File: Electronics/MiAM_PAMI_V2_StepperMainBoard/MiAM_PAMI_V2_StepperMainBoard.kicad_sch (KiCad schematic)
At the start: 31 parts, among them J1 Conn_01x11_Male, J2 Conn_01x03_Male, J3 Conn_01x03_Male, U1 ESP32-DEVKITC-32U, U2 3V3, U3 MT3608, U4 LM7805_TO220

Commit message: Fix pcb & add driver board
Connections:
- net +3V3: now also J1.11 (Pin_11); no longer J1.10 (Pin_10)
- net DIR_1: now also J1.7 (Pin_7); no longer J1.6 (Pin_6)
- net DIR_2: now also J1.9 (Pin_9); no longer J1.8 (Pin_8)
- net GND: now also J1.2 (Pin_2); no longer J1.11 (Pin_11)
- net MS1: now also J1.3 (Pin_3); no longer J1.2 (Pin_2)
- net MS2: now also J1.4 (Pin_4); no longer J1.3 (Pin_3)
- net MS3: now also J1.5 (Pin_5); no longer J1.4 (Pin_4)
- net NOT_MOT_EN: now also J1.10 (Pin_10); no longer J1.9 (Pin_9)
- net STEP_1: now also J1.6 (Pin_6); no longer J1.5 (Pin_5)
- net STEP_2: now also J1.8 (Pin_8); no longer J1.7 (Pin_7)

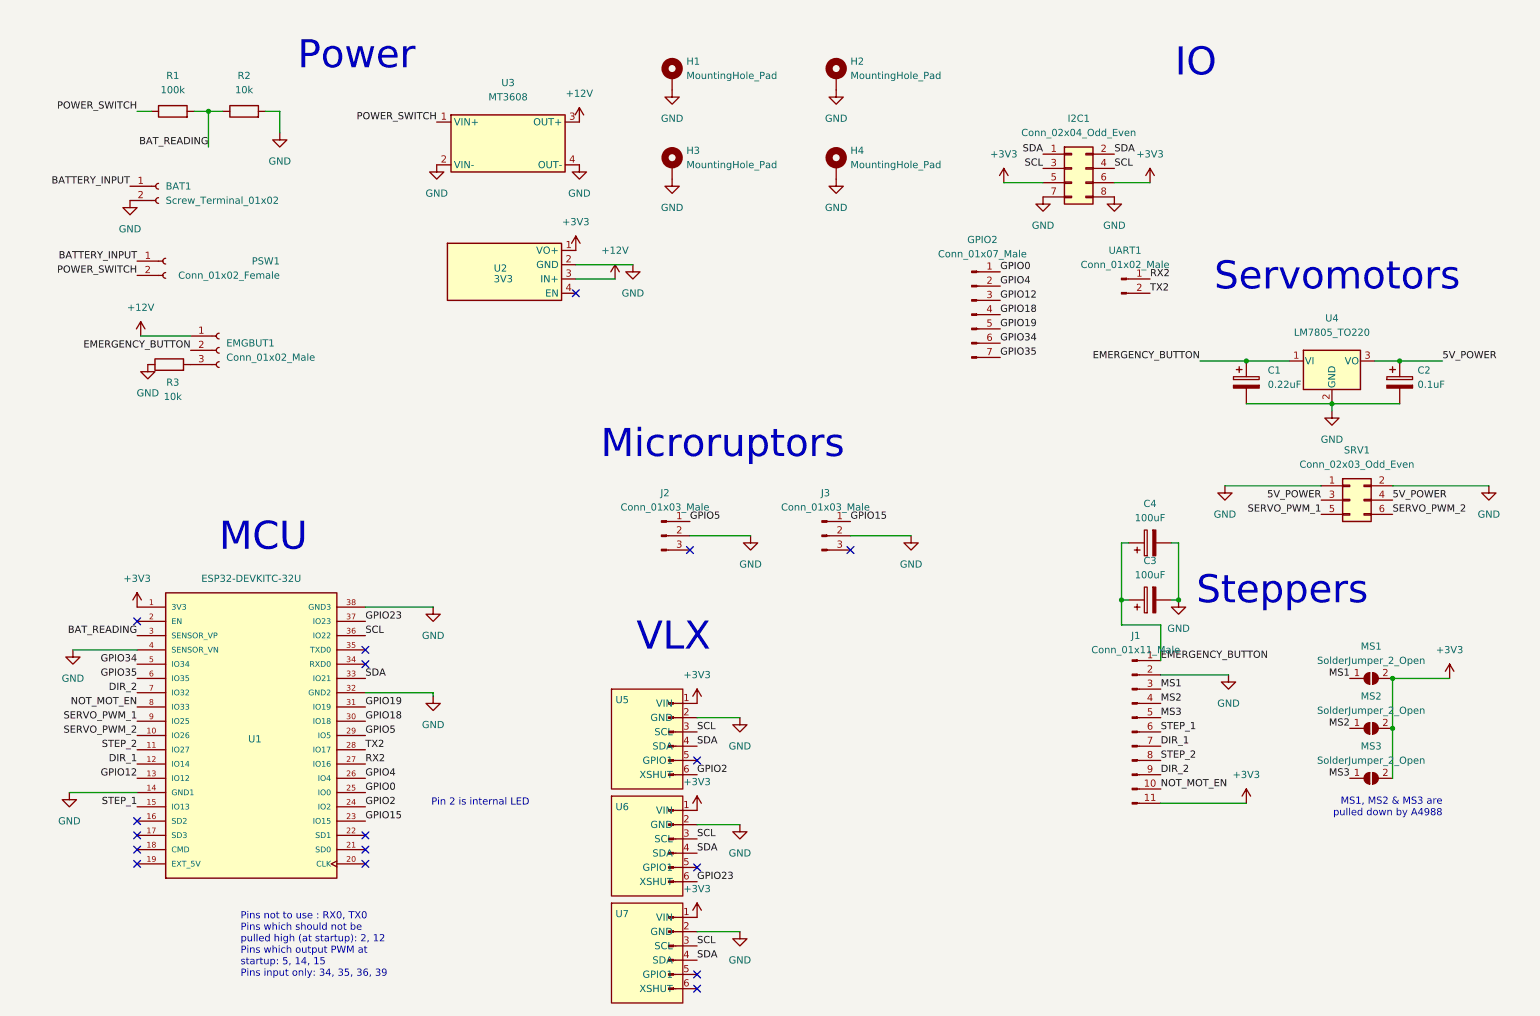
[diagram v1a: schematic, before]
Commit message: Put stepper driver on main board
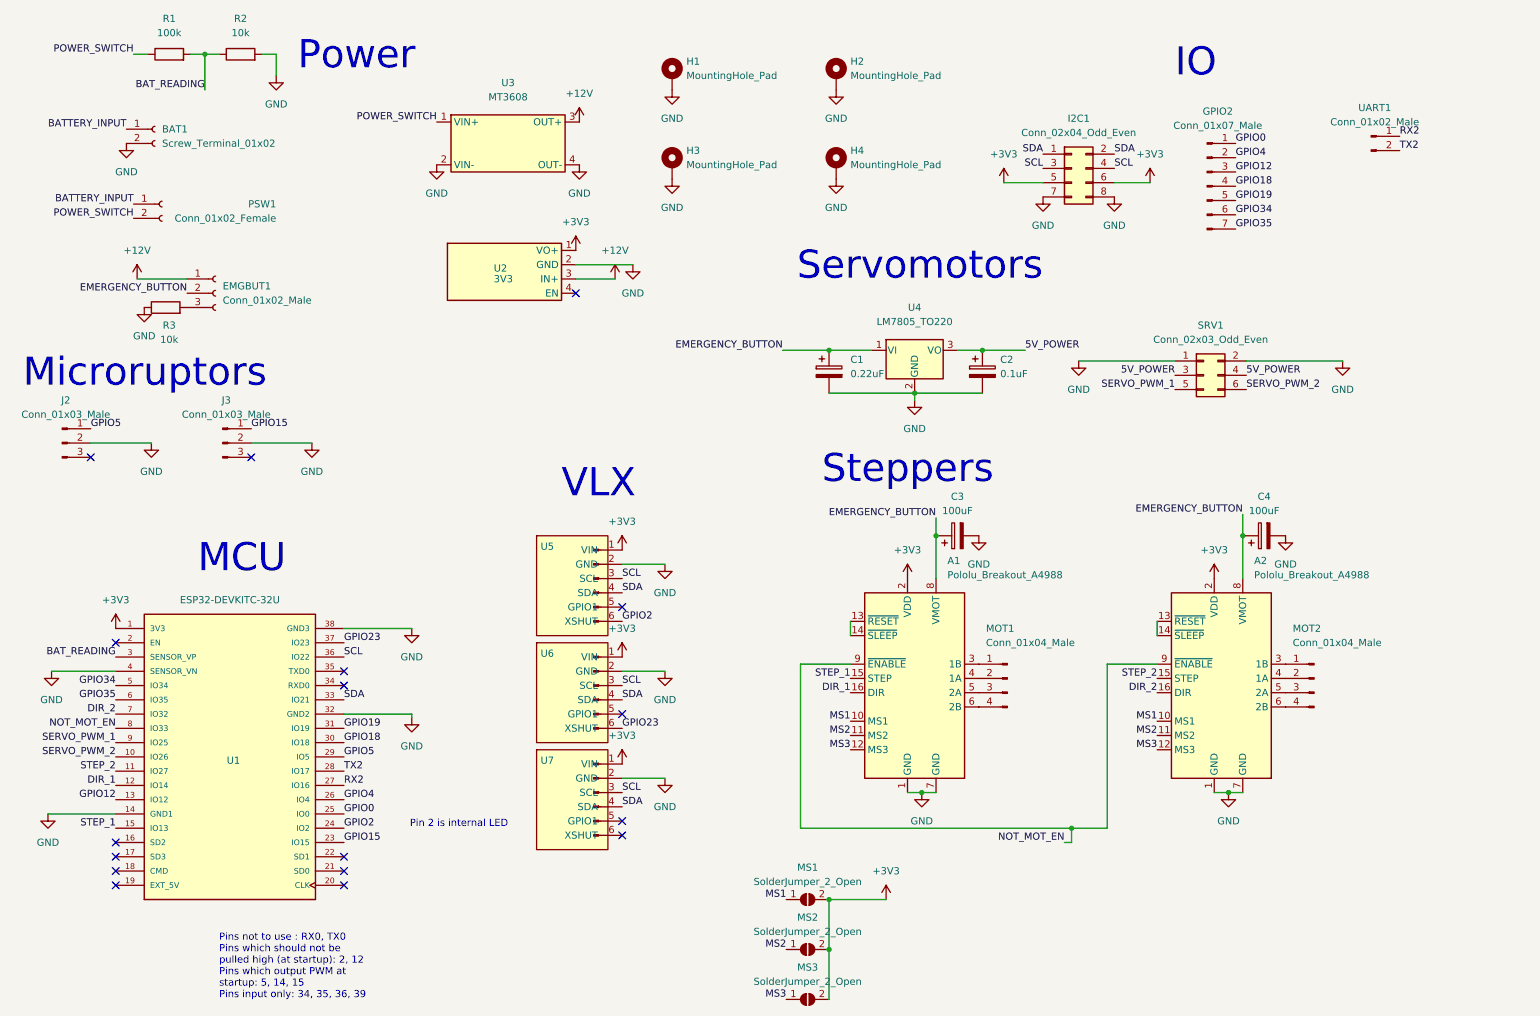
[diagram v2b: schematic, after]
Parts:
- removed J1: Conn_01x11_Male, Connector_PinSocket_2.54mm:PinSocket_1x11_P2.54mm_Vertical, symbol Connector:Conn_01x11_Male
- added A1, A2: Pololu_Breakout_A4988, Module:Pololu_Breakout-16_15.2x20.3mm, symbol Driver_Motor:Pololu_Breakout_A4988
- added MOT1, MOT2: Conn_01x04_Male, Connector_PinHeader_2.54mm:PinHeader_1x04_P2.54mm_Vertical, symbol Connector:Conn_01x04_Male
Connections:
- net +3V3: now also A1.2 (VDD), A2.2 (VDD)
- net DIR_1: now also A1.16 (DIR)
- net DIR_2: now also A2.16 (DIR)
- net EMERGENCY_BUTTON: now also A1.8 (VMOT), A2.8 (VMOT)
- net GND: now also A1.1 (GND), A1.7 (GND), A2.1 (GND), A2.7 (GND)
- net MS1: now also A1.10 (MS1), A2.10 (MS1)
- net MS2: now also A1.11 (MS2), A2.11 (MS2)
- net MS3: now also A1.12 (MS3), A2.12 (MS3)
- net NOT_MOT_EN: now also A1.9 (~{ENABLE}), A2.9 (~{ENABLE})
- net STEP_1: now also A1.15 (STEP)
- net STEP_2: now also A2.15 (STEP)
- new net: A2.3 (1B), MOT2.1 (Pin_1)
- new net: A2.4 (1A), MOT2.2 (Pin_2)
- new net: A2.5 (2A), MOT2.3 (Pin_3)
- new net: A2.6 (2B), MOT2.4 (Pin_4)
- new net: A1.13 (~{RESET}), A1.14 (~{SLEEP})
- new net: A1.3 (1B), MOT1.1 (Pin_1)
- new net: A1.4 (1A), MOT1.2 (Pin_2)
- new net: A1.5 (2A), MOT1.3 (Pin_3)
- new net: A1.6 (2B), MOT1.4 (Pin_4)
- new net: A2.13 (~{RESET}), A2.14 (~{SLEEP})
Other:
- note removed: "MS1, MS2 & MS3 are pulled down by A4988"
- moved on the sheet: BAT1, C1, C2, C3, C4, EMGBUT1, GPIO2, J2, J3, PSW1, R1, R2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

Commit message: Initial commit PAMI V3
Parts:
- removed C1: 0.22uF, Capacitor_THT:CP_Radial_D4.0mm_P2.00mm, symbol Device:C_Polarized
- removed C2: 0.1uF, Capacitor_THT:CP_Radial_D4.0mm_P2.00mm, symbol Device:C_Polarized
- removed PSW1: Conn_01x02_Female, Connector_JST:JST_PH_B2B-PH-K_1x02_P2.00mm_Vertical, symbol Connector:Conn_01x02_Female
- removed U4: LM7805_TO220, Package_TO_SOT_THT:TO-220-3_Horizontal_TabDown, symbol Regulator_Linear:LM7805_TO220
- added SW1: SW_DPDT_x2, MiAM_ESP32_Footprints:SS-12D11, symbol Switch:SW_DPDT_x2
- added U4: 3V3, MiAM_ESP32_Footprints:VoltageRegulator, symbol MiAM_ESP32:VoltageRegulator
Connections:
- net 5V_POWER: now also U4.1 (VO+)
- net BATTERY_INPUT: now also SW1.3 (C)
- net EMERGENCY_BUTTON: now also U4.3 (IN+)
- net GND: now also U4.2 (GND)
- net POWER_SWITCH: now also SW1.2 (B)
- no-connect marks 17 -> 19
